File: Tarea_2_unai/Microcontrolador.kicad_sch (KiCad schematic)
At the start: 5 parts, among them IC1 ESP32-C3-MINI-1-N4

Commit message: actualización completa
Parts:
- added J2: Conn_01x02_Pin, PinHeader_1x04_P2.54mm_Vertical, symbol Connector:Conn_01x02_Pin
- IC1: footprint ESP32C3MINI1N4 -> ESP32-C3-MINI-1-N4
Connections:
- net GND_REF: now also J2.1 (Pin_1); no longer IC1.5 (IO2)
- net at C1.1, R1.1: now also J2.2 (Pin_2); no longer IC1.7 (NC_2)
- no-connect marks 56 -> 58
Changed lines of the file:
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@@
+	)
+	(junction
+		(at 68.58 72.39)
+		(diameter 0)
+		(color 0 0 0 0)
 	)
 	(junction
@@
 		(color 0 0 0 0)
 	)
-	(junction
-		(at 68.58 81.28)
-		(diameter 0)
-		(color 0 0 0 0)
-	)
 	(no_connect
 		(at 119.38 74.93)
@@
 	)
 	(no_connect
+		(at 119.38 36.83)
+	)
+	(no_connect
 		(at 152.4 95.25)
 	)
@@
 	)
 	(no_connect
+		(at 119.38 31.75)
+	)
+	(no_connect
 		(at 152.4 72.39)
 	)
@@
 	(wire
 		(pts
+			(xy 71.12 58.42) (xy 71.12 67.31)
+		)
+		(stroke
+			(width 0)
+			(type default)
+		)
+	)
+	(wire
+		(pts
 			(xy 118.11 26.67) (xy 119.38 26.67)
 		)
@@
 	(wire
 		(pts
-			(xy 119.38 36.83) (xy 100.33 36.83)
-		)
-		(stroke
-			(width 0)
-			(type default)
-		)
-	)
-	(wire
-		(pts
 			(xy 118.11 25.4) (xy 85.09 25.4)
 		)
@@
 	(wire
 		(pts
-			(xy 100.33 36.83) (xy 100.33 81.28)
-		)
-		(stroke
-			(width 0)
-			(type default)
-		)
-	)
-	(wire
-		(pts
 			(xy 85.09 58.42) (xy 85.09 29.21)
 		)
@@
 	(wire
 		(pts
-			(xy 68.58 72.39) (xy 68.58 81.28)
-		)
-		(stroke
-			(width 0)
-			(type default)
-		)
-	)
-	(wire
-		(pts
-			(xy 119.38 31.75) (xy 88.9 31.75)
+			(xy 68.58 69.85) (xy 68.58 72.39)
+		)
+		(stroke
+			(width 0)
+			(type default)
+		)
+	)
+	(wire
+		(pts
+			(xy 68.58 72.39) (xy 68.58 82.55)
 		)
 		(stroke
@@
 	(wire
 		(pts
-			(xy 71.12 58.42) (xy 71.12 66.04)
-		)
-		(stroke
-			(width 0)
-			(type default)
-		)
-	)
-	(wire
-		(pts
-			(xy 100.33 81.28) (xy 68.58 81.28)
-		)
-		(stroke
-			(width 0)
-			(type default)
-		)
-	)
-	(wire
-		(pts
 			(xy 30.48 97.79) (xy 68.58 97.79)
 		)
@@
 	(wire
 		(pts
-			(xy 88.9 31.75) (xy 88.9 66.04)
-		)
-		(stroke
-			(width 0)
-			(type default)
-		)
-	)
-	(wire
-		(pts
-			(xy 68.58 81.28) (xy 68.58 82.55)
-		)
-		(stroke
-			(width 0)
-			(type default)
-		)
-	)
-	(wire
-		(pts
-			(xy 88.9 66.04) (xy 71.12 66.04)
+			(xy 64.77 69.85) (xy 68.58 69.85)
+		)
+		(stroke
+			(width 0)
+			(type default)
+		)
+	)
+	(wire
+		(pts
+			(xy 71.12 67.31) (xy 64.77 67.31)
 		)
 		(stroke
@@
 			)
 		)
-		(property "Footprint" "ESP32C3MINI1N4"
+		(property "Footprint" "ESP32-C3-MINI-1-N4"
 			(at 148.59 116.51 0)
 			(hide yes)
@@
 					(unit 1)
 				)
+			)
+		)
+	)
+	(symbol
+		(lib_id "Connector:Conn_01x02_Pin")
+		(at 59.69 67.31 0)
+		(unit 1)
+		(body_style 1)
+		(exclude_from_sim no)
+		(in_bom yes)
+		(on_board yes)
+		(in_pos_files yes)
+		(dnp no)
+		(fields_autoplaced yes)
+		(property "Reference" "J2"
+			(at 60.325 62.23 0)
+			(show_name no)
+			(do_not_autoplace no)
+			(effects
+				(font
+					(size 1.27 1.27)
+				)
+			)
+		)
+		(property "Value" "Conn_01x02_Pin"
+			(at 60.325 64.77 0)
+			(show_name no)
+			(do_not_autoplace no)
+			(effects
+				(font
+					(size 1.27 1.27)
+				)
+			)
+		)
+		(property "Footprint" "PinHeader_1x04_P2.54mm_Vertical"
+			(at 59.69 67.31 0)
+			(hide yes)
+			(show_name no)
+			(do_not_autoplace no)
+			(effects
+				(font
+					(size 1.27 1.27)
+				)
+			)
+		)
+		(property "Datasheet" ""
+			(at 59.69 67.31 0)
+			(hide yes)
+			(show_name no)
+			(do_not_autoplace no)
+			(effects
+				(font
+					(size 1.27 1.27)
+				)
+			)
+		)
+		(property "Description" "Generic connector, single row, 01x02, script generated"
+			(at 59.69 67.31 0)
+			(hide yes)
+			(show_name no)
+			(do_not_autoplace no)
+			(effects
+				(font
+					(size 1.27 1.27)
+				)
+			)
+		)
+		(pin "2"
+		)
+		(pin "1"
+		)
+		(instances
+			(project "Tarea_2_unai"
+				(path "/2324ac65-aae7-4e51-a8e4-9d93764ceb90/5cbed766-6105-4833-8b7f-4c3640c40f4a"
+					(reference "J2")
+					(unit 1)
+				)

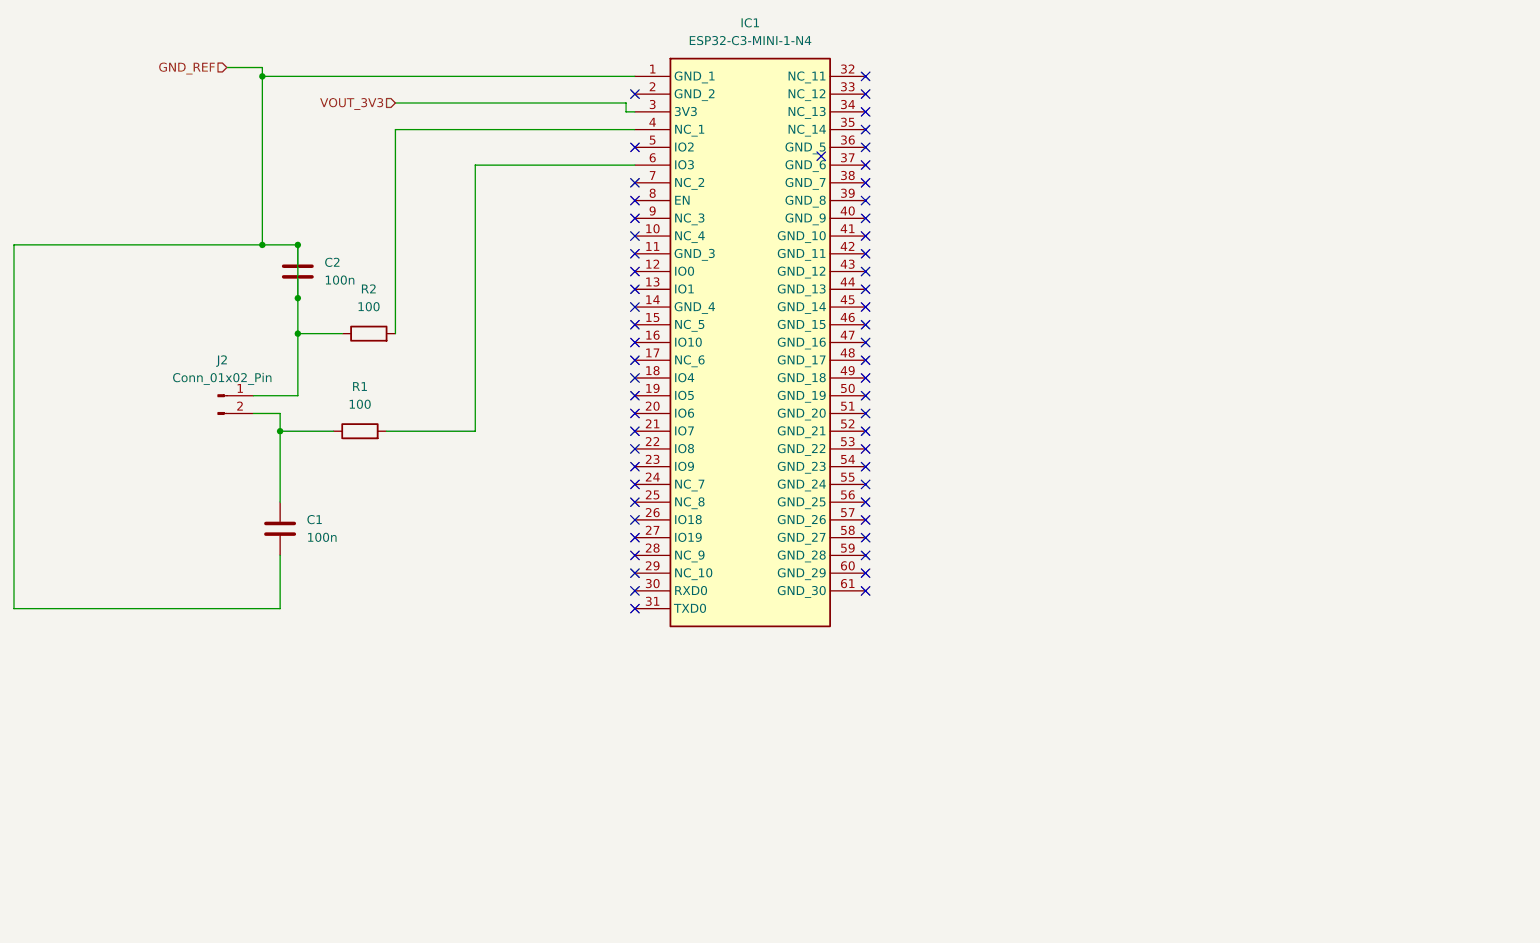
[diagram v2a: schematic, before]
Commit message: Tarea_3
Falta el enrutado y configuraciones Configurar el Clearance a 0.2mm y Track Width
/ Track Distance mínimos a 0.25mm
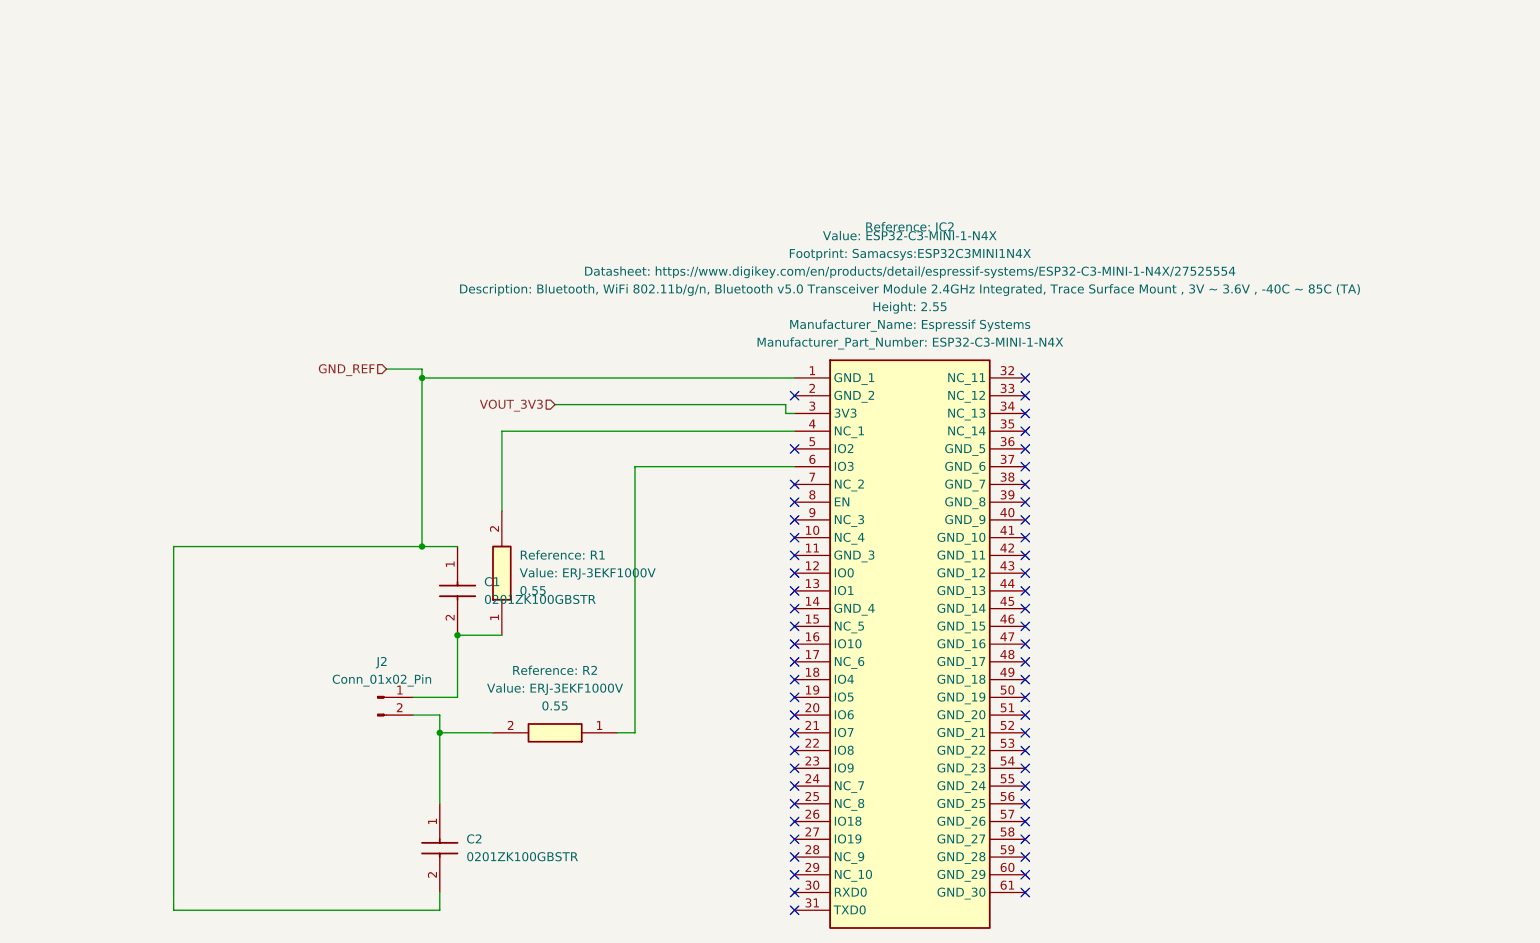
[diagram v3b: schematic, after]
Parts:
- removed C1, C2: 100n, 0201ZK100GBSTR, symbol Device:C
- removed IC1: ESP32-C3-MINI-1-N4, ESP32-C3-MINI-1-N4, symbol ESP32-C3-MINI-1-N4:ESP32-C3-MINI-1-N4
- removed R1, R2: 100, ERJ-3EKF1000V, symbol Device:R
- added C1, C2: 0201ZK100GBSTR, CAPC0603X28N, symbol 0201ZK100GBSTR:0201ZK100GBSTR
- added IC2: ESP32-C3-MINI-1-N4X, Samacsys:ESP32C3MINI1N4X, symbol Samacsys:ESP32-C3-MINI-1-N4X
- added R1, R2: ERJ-3EKF1000V, Samacsys:RESC1608X55N, symbol Samacsys:ERJ-3EKF1000V
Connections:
- net GND_REF: now also C1.1, C2.2, IC2.1 (GND_1); no longer J2.1 (Pin_1)
- net VOUT_3V3: now also IC2.3 (3V3)
- net at J2.2 (Pin_2): now also C2.1, R2.2
- new net: C1.2, J2.1 (Pin_1), R1.1
- new net: IC2.4 (NC_1), R1.2
- new net: IC2.6 (IO3), R2.1
- no-connect marks 58 -> 57
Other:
- moved on the sheet: J2

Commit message: zona_fill
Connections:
- net GND_REF: now also IC2.11 (GND_3), IC2.14 (GND_4), IC2.2 (GND_2)
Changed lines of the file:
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@@
 	(paper "A4")
 	(junction
+		(at 142.24 64.77)
+		(diameter 0)
+		(color 0 0 0 0)
+	)
+	(junction
+		(at 137.16 64.77)
+		(diameter 0)
+		(color 0 0 0 0)
+	)
+	(junction
 		(at 91.44 115.57)
 		(diameter 0)
@@
 	)
 	(junction
+		(at 135.89 64.77)
+		(diameter 0)
+		(color 0 0 0 0)
+	)
+	(junction
 		(at 88.9 64.77)
 		(diameter 0)
@@
 	(wire
 		(pts
+			(xy 135.89 64.77) (xy 137.16 64.77)
+		)
+		(stroke
+			(width 0)
+			(type default)
+		)
+	)
+	(wire
+		(pts
 			(xy 140.97 69.85) (xy 142.24 69.85)
 		)
@@
 	(wire
 		(pts
+			(xy 142.24 67.31) (xy 142.24 64.77)
+		)
+		(stroke
+			(width 0)
+			(type default)
+		)
+	)
+	(wire
+		(pts
 			(xy 140.97 68.58) (xy 107.95 68.58)
 		)
@@
 	(wire
 		(pts
+			(xy 137.16 90.17) (xy 137.16 64.77)
+		)
+		(stroke
+			(width 0)
+			(type default)
+		)
+	)
+	(wire
+		(pts
 			(xy 88.9 63.5) (xy 88.9 88.9)
 		)
@@
 	(wire
 		(pts
+			(xy 137.16 64.77) (xy 142.24 64.77)
+		)
+		(stroke
+			(width 0)
+			(type default)
+		)
+	)
+	(wire
+		(pts
 			(xy 140.97 69.85) (xy 140.97 68.58)
 		)
@@
 	(wire
 		(pts
+			(xy 142.24 97.79) (xy 135.89 97.79)
+		)
+		(stroke
+			(width 0)
+			(type default)
+		)
+	)
+	(wire
+		(pts
 			(xy 119.38 115.57) (xy 119.38 77.47)
 		)
@@
 	(wire
 		(pts
-			(xy 88.9 64.77) (xy 142.24 64.77)
+			(xy 142.24 90.17) (xy 137.16 90.17)
+		)
+		(stroke
+			(width 0)
+			(type default)
+		)
+	)
+	(wire
+		(pts
+			(xy 88.9 64.77) (xy 135.89 64.77)
 		)
 		(stroke
@@
 		)
 		(stroke
+			(width 0)
+			(type default)
+		)
+	)
+	(wire
+		(pts
+			(xy 135.89 97.79) (xy 135.89 64.77)
+		)
+		(stroke
